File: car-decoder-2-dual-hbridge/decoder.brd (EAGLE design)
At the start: 98.8 x 80 mm, 46 parts, among them U1 MPC17531-ES, U2 RFM69CW, U3 MCP73831, U4 ATMEGA328P, U5 MPC17531-ES, U6 MIC5219 3.3V, Y1 16MHZ

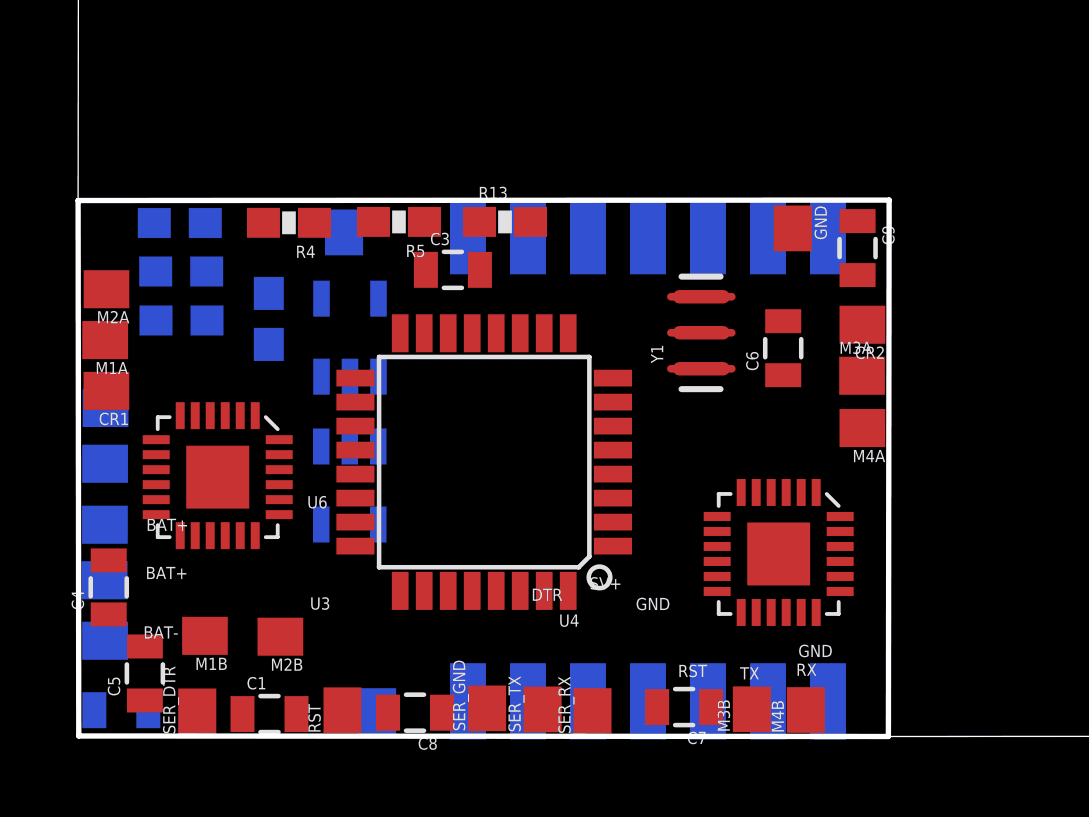
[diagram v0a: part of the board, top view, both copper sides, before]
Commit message: New layout for RFM69HC
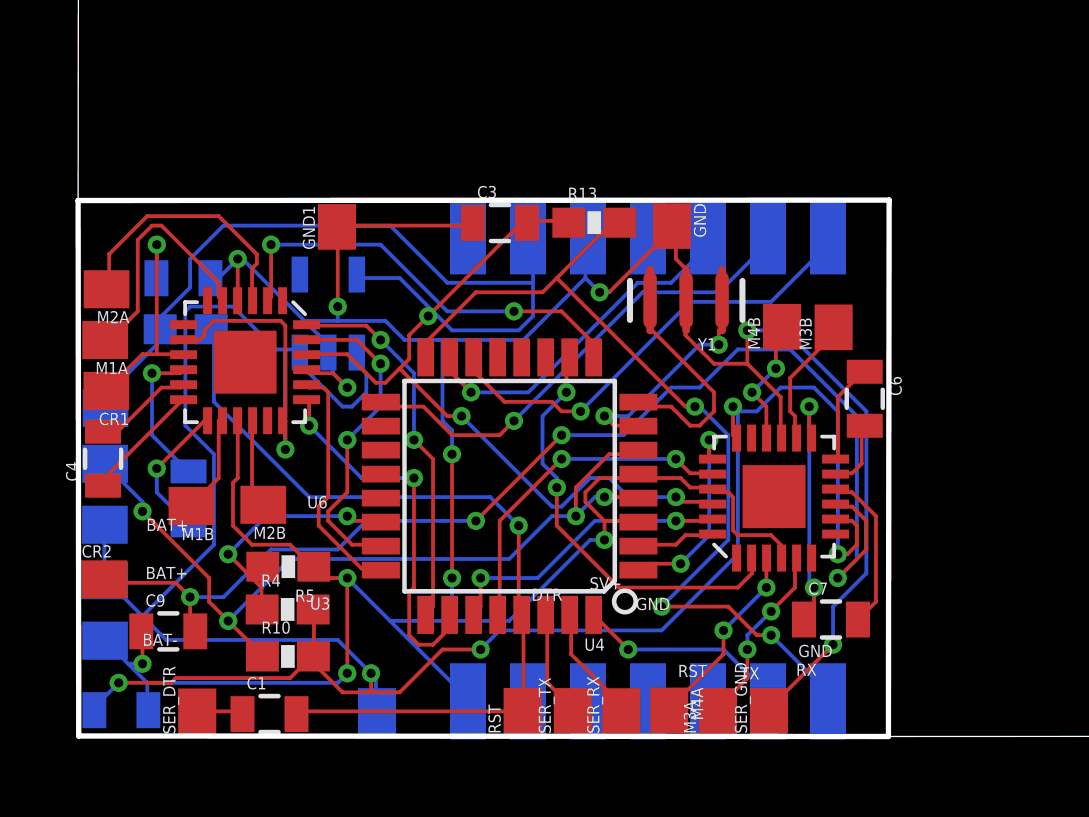
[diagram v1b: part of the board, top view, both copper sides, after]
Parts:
- removed R12: 0, SparkFun-Resistors:0603-RES
- removed R3: 2K, SparkFun-Resistors:0603-RES
- removed U3: MCP73831, SparkFun-PowerIC:SOT23-5
- moved CR2 26.7 mm to (2.07, 5.19), turned to 270 degrees
- moved C9 26.3 mm to (4.19, 3.46), turned to 0 degrees
- moved C8 16.4 mm to (4.70, 15.2), flipped to the bottom, turned to 0 degrees
- moved M3B 13.0 mm to (26.4, 13.6)
- moved R4 12.9 mm to (8.17, 4.19), turned to 0 degrees
- moved M4B 12.8 mm to (24.7, 13.6)
- moved M3A 12.2 mm to (22.5, 0.81), turned to 0 degrees
- moved R5 12.1 mm to (8.19, 5.62)
- moved R10 11.7 mm to (8.18, 2.62), flipped to the top, turned to 0 degrees
- moved M4A 11.4 mm to (20.9, 0.83), turned to 180 degrees
- moved SER_GND 9.39 mm to (24.2, 0.82)
- moved C5 6.01 mm to (4.87, 7.89), flipped to the bottom
- moved RST 6.00 mm to (16.0, 0.81)
- moved C7 5.70 mm to (26.3, 3.86), turned to 0 degrees
- moved M2B 4.43 mm to (7.36, 7.68)
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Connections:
- removed net N$11: R3.1, U3.5
- removed net N$9: SER_V+.1, U3.4
- net A6: no longer U3.1
- net BAT+: now also SER_V+.1; no longer U3.3
- net GND: no longer R3.2, U3.2
- net N$8: no longer R12.2
- net VCC: no longer R12.1
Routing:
- net GND: track 0.00 -> 117.7 mm, vias 0 -> 12
- net BAT+: track 0.00 -> 89.8 mm, vias 0 -> 6
- net VCC: track 0.00 -> 53.7 mm, vias 0 -> 3
- net N$21: track 0.00 -> 40.1 mm, vias 0 -> 4
- net MISO: track 0.00 -> 30.2 mm, vias 0 -> 3
- net N$5: track 0.00 -> 28.2 mm, vias 0 -> 1
- net N$8: track 0.00 -> 27.6 mm, vias 0 -> 4
- net SCK: track 0.00 -> 16.3 mm, vias 0 -> 1
- net SS: track 0.00 -> 15.4 mm, vias 0 -> 1
- net D5: track 0.00 -> 14.5 mm, vias 0 -> 2
- net D6: track 0.00 -> 14.3 mm, vias 0 -> 2
- net A2: track 0.00 -> 12.7 mm, vias 0 -> 2
- net A3: track 0.00 -> 12.6 mm, vias 0 -> 2
- net MOSI: track 0.00 -> 11.7 mm, vias 0 -> 1
- net A5: track 0.00 -> 11.3 mm, vias 0 -> 2
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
